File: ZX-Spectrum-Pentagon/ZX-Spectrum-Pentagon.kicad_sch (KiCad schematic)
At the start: 0 parts

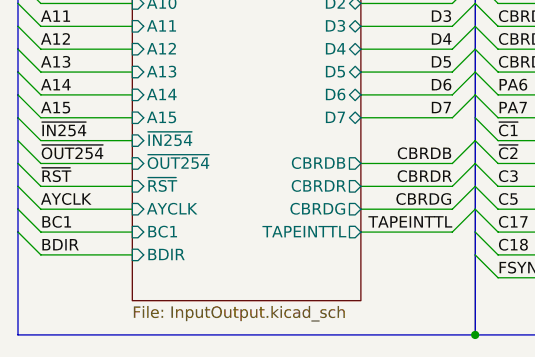
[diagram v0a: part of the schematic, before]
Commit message: add ~{RESET} signal to keyboard
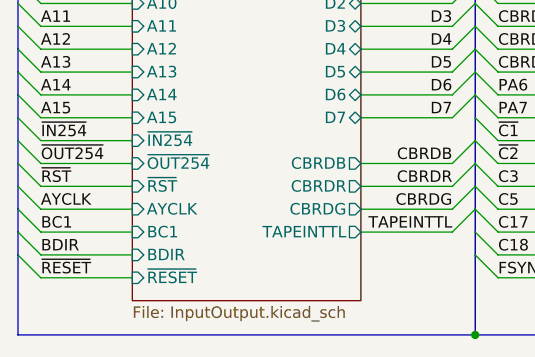
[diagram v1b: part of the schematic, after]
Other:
- sheet InputOutput ports: added ~{RESET}; removed none
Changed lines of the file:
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@@
     (stroke (width 0) (type default) (color 0 0 0 0))
   )
+  (bus_entry (at 25.4 187.96) (size 2.54 2.54)
+    (stroke (width 0) (type default) (color 0 0 0 0))
+  )
   (bus_entry (at 127 114.3) (size -2.54 2.54)
     (stroke (width 0) (type default) (color 0 0 0 0))
@@
     (stroke (width 0) (type default) (color 0 0 0 0))
   )
-  (bus (pts (xy 25.4 185.42) (xy 25.4 196.85))
+  (bus (pts (xy 25.4 185.42) (xy 25.4 187.96))
     (stroke (width 0) (type default) (color 0 0 0 0))
   )
@@
     (stroke (width 0) (type default) (color 0 0 0 0))
   )
+  (wire (pts (xy 27.94 190.5) (xy 38.1 190.5))
+    (stroke (width 0) (type default) (color 0 0 0 0))
+  )
   (bus (pts (xy 127 69.85) (xy 127 71.12))
     (stroke (width 0) (type default) (color 0 0 0 0))
@@
     (stroke (width 0) (type default) (color 0 0 0 0))
   )
+  (bus (pts (xy 25.4 187.96) (xy 25.4 196.85))
+    (stroke (width 0) (type default) (color 0 0 0 0))
+  )
   (wire (pts (xy 78.74 152.4) (xy 88.9 152.4))
     (stroke (width 0) (type default) (color 0 0 0 0))
@@
     (effects (font (size 1.27 1.27)) (justify right bottom))
   )
+  (label "~{RESET}" (at 27.94 190.5 0)
+    (effects (font (size 1.27 1.27)) (justify left bottom))
+  )
   (label "C3" (at 78.74 180.34 0)
     (effects (font (size 1.27 1.27)) (justify left bottom))
@@
       (effects (font (size 1.27 1.27)) (justify right))
     )
+    (pin "~{RESET}" input (at 38.1 190.5 180)
+      (effects (font (size 1.27 1.27)) (justify left))
+    )
   )
   (sheet (at 88.9 104.14) (size 25.4 27.94) (fields_autoplaced)
@@
       (reference "#PWR0102") (unit 1) (value "VCC") (footprint "")
     )
-    (path "/00000000-0000-0000-0000-000062a08194/0e9cb254-d5a6-43df-b938-d4e89e7c4f1b"
-      (reference "#PWR0103") (unit 1) (value "GND") (footprint "")
-    )
     (path "/00000000-0000-0000-0000-000062a08194/c31e7ab1-f89e-4888-8329-6b12abe8b2da"
       (reference "#PWR0104") (unit 1) (value "VCC") (footprint "")
@@
     )
     (path "/00000000-0000-0000-0000-000062a08194/ac0214e0-cfb9-4b53-9214-9139dd989c7d"
-      (reference "JIOKB1") (unit 1) (value "KDATA") (footprint "Connector_PinHeader_2.54mm:PinHeader_1x07_P2.54mm_Vertical")
+      (reference "JIOKB1") (unit 1) (value "KDATA") (footprint "Connector_PinHeader_2.54mm:PinHeader_1x08_P2.54mm_Vertical")
     )
     (path "/00000000-0000-0000-0000-000062a08194/de775720-f7f2-4e8e-8eb2-c9141e64fe25"

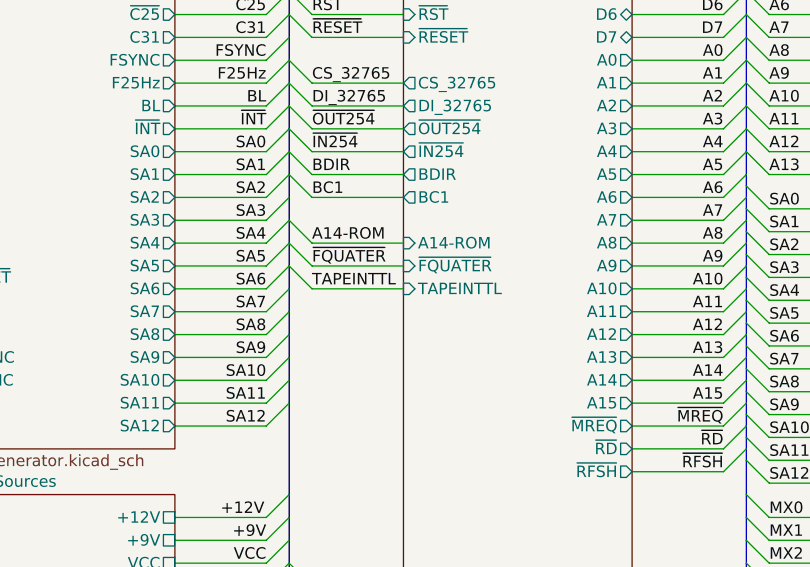
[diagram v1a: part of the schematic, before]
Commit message: add second level delete TYPETTL
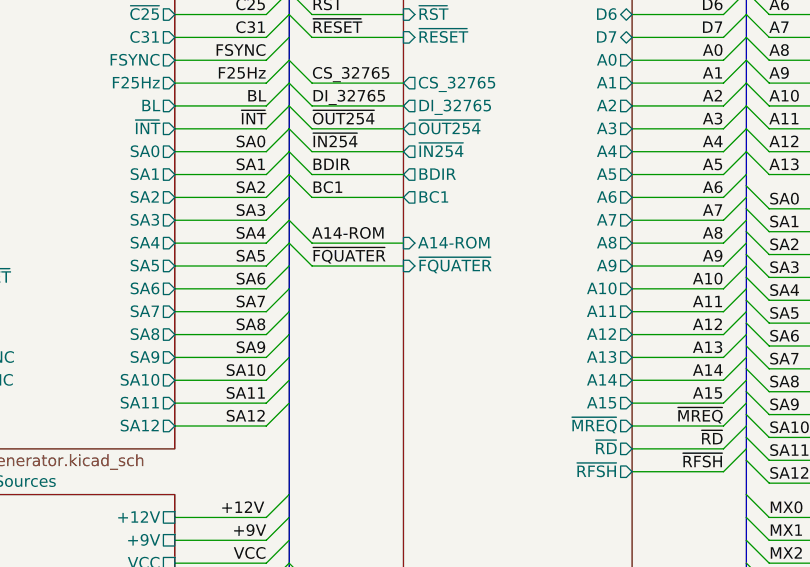
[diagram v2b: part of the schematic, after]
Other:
- sheet CPU ports: added none; removed TAPEINTTL
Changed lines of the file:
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@@
-    (stroke (width 0) (type default) (color 0 0 0 0))
-  )
-  (bus_entry (at 76.2 60.96) (size 2.54 2.54)
     (stroke (width 0) (type default) (color 0 0 0 0))
   )
@@
     (stroke (width 0) (type default) (color 0 0 0 0))
   )
-  (wire (pts (xy 78.74 63.5) (xy 88.9 63.5))
-    (stroke (width 0) (type default) (color 0 0 0 0))
-  )
   (wire (pts (xy 63.5 132.08) (xy 73.66 132.08))
     (stroke (width 0) (type default) (color 0 0 0 0))
@@
   )
   (label "A15" (at 27.94 172.72 0)
-    (effects (font (size 1.27 1.27)) (justify left bottom))
-  )
-  (label "TAPEINTTL" (at 78.74 63.5 0)
     (effects (font (size 1.27 1.27)) (justify left bottom))
   )
@@
       (effects (font (size 1.27 1.27)) (justify left))
     )
-    (pin "TAPEINTTL" input (at 88.9 63.5 180)
-      (effects (font (size 1.27 1.27)) (justify left))
-    )

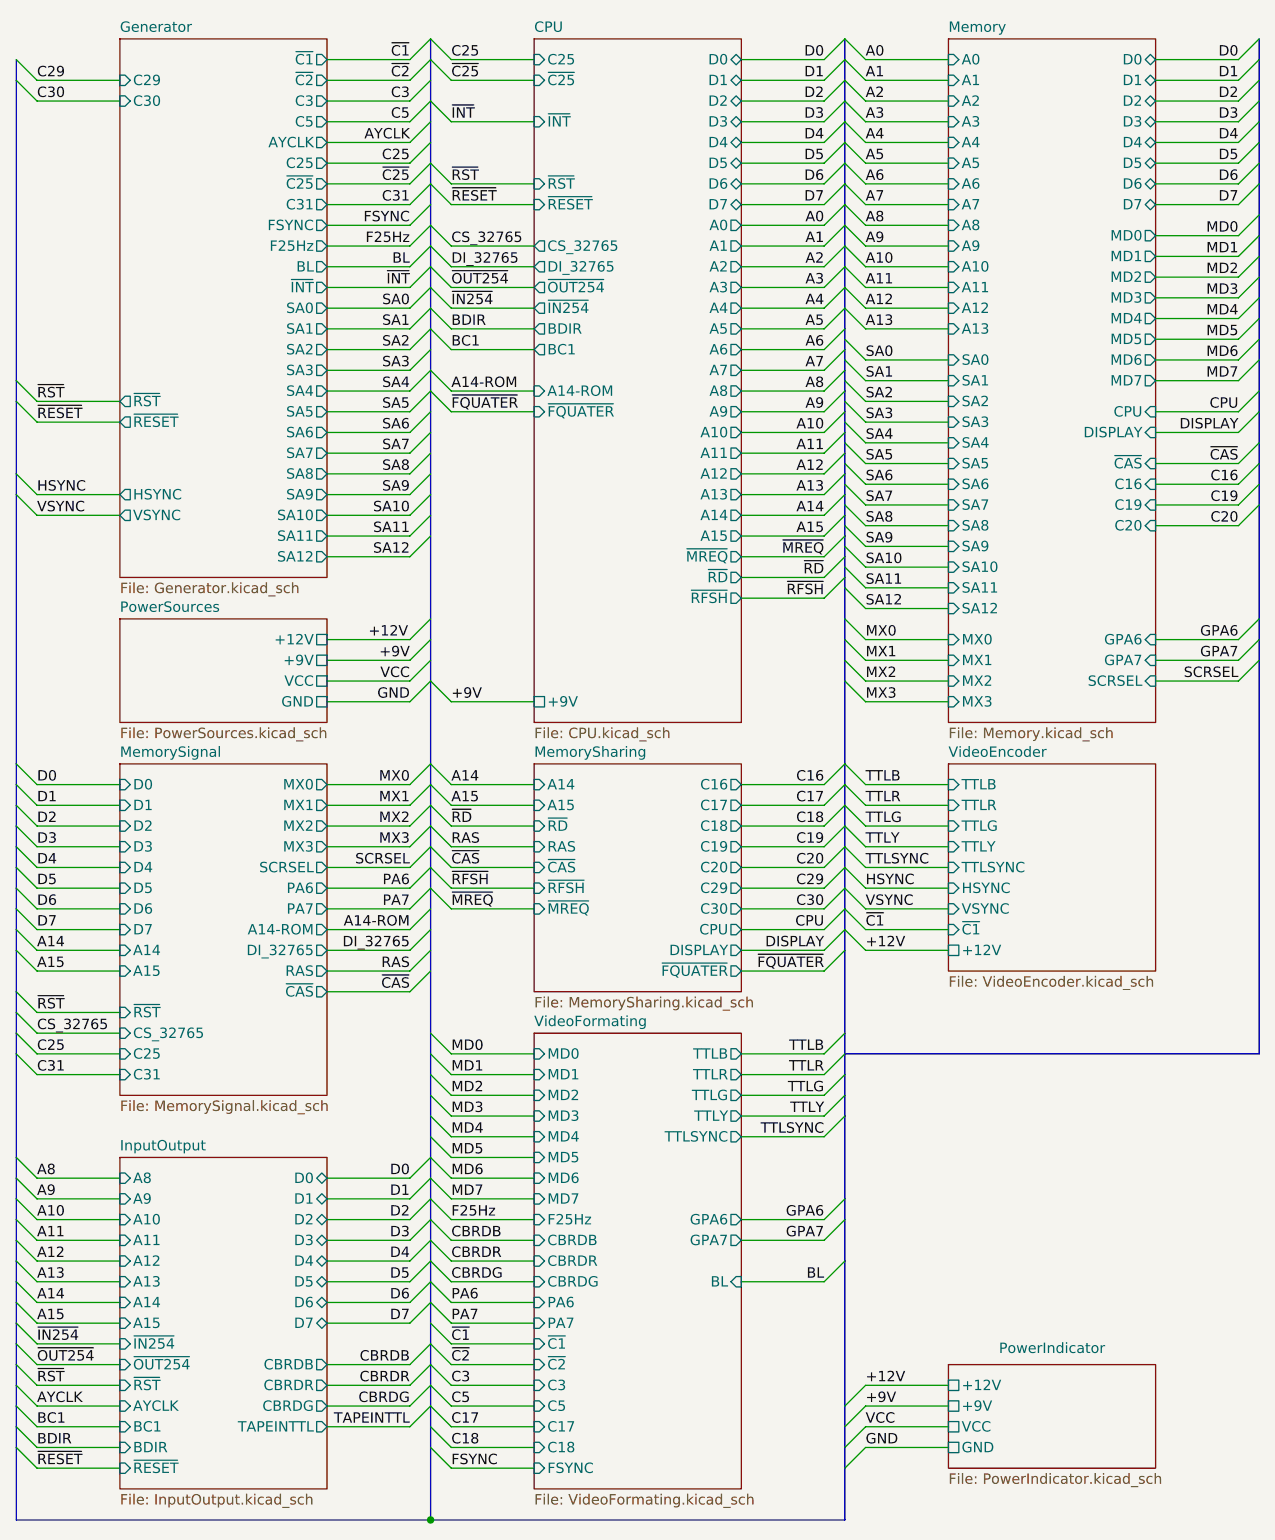
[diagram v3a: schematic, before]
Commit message: migrate ZX-Spectrum-Keyboard_Switch
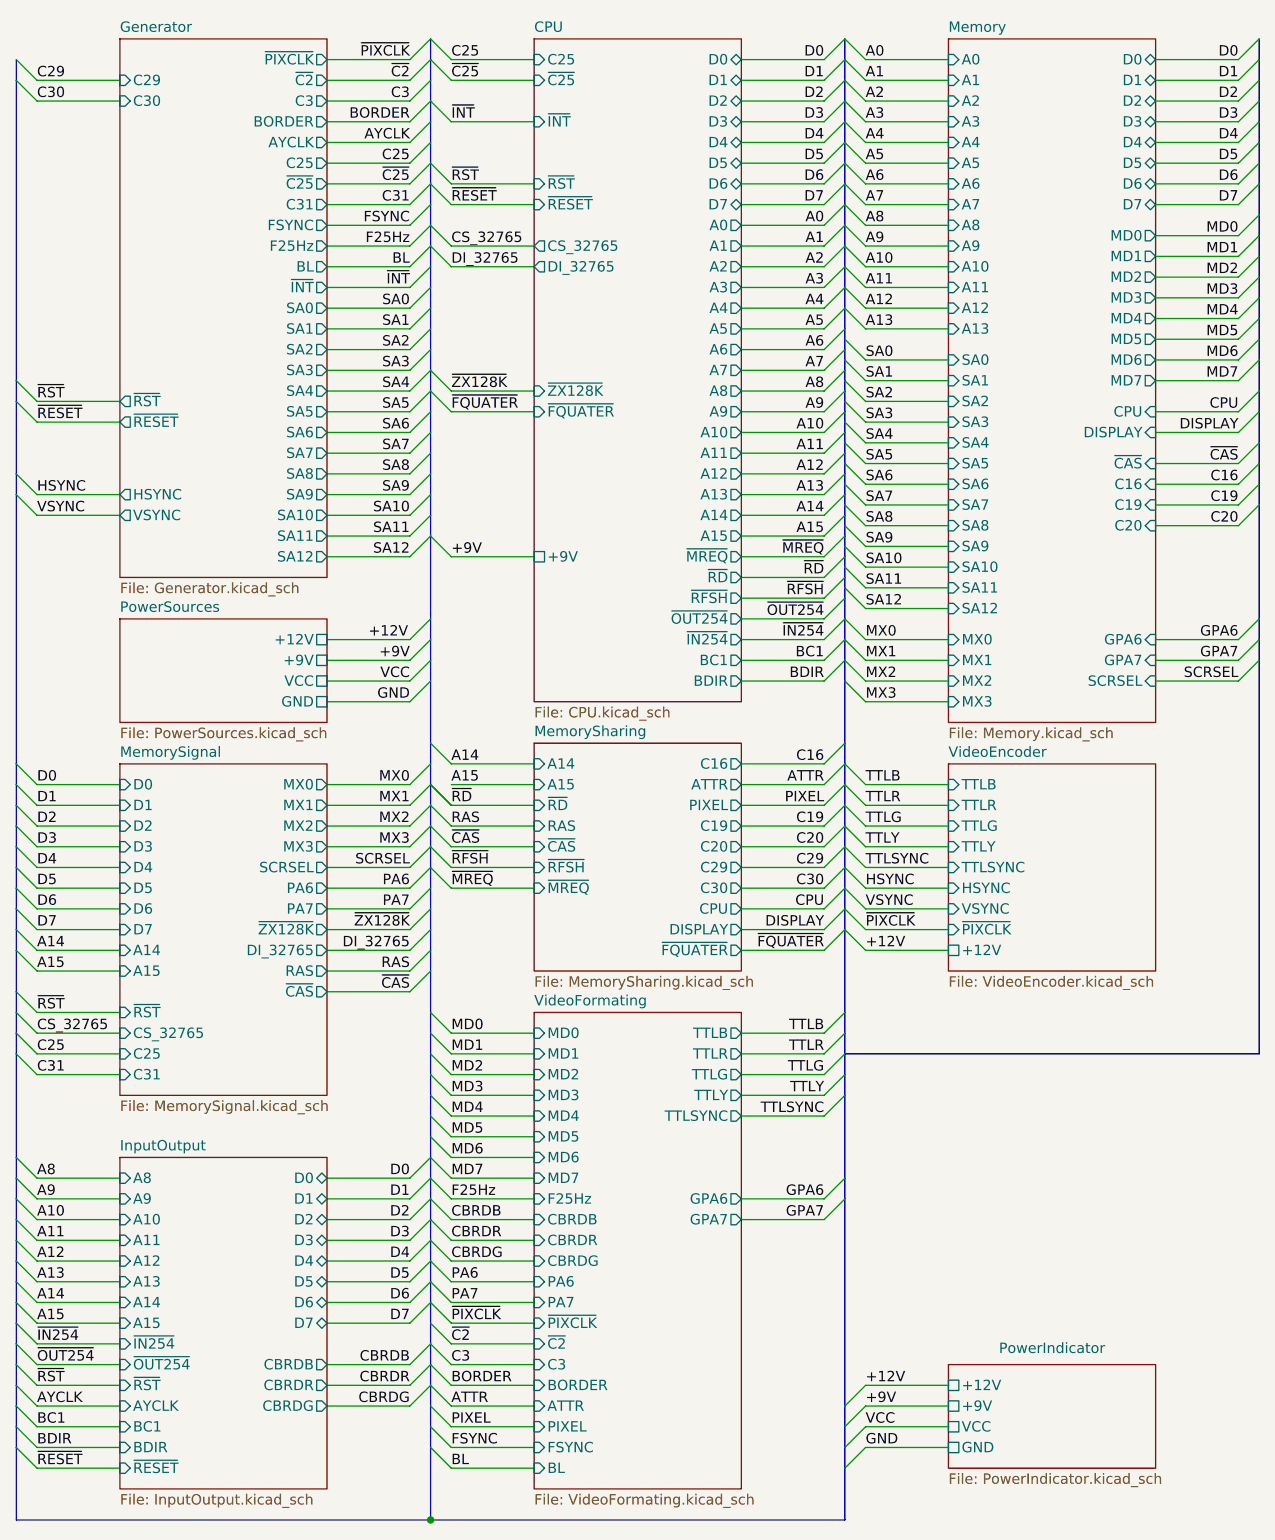
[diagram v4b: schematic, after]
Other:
- sheet CPU ports: added ~{ZX128K}; removed A14-ROM
- sheet Generator ports: added BORDER, ~{PIXCLK}; removed C5, ~{C1}
- sheet InputOutput ports: added none; removed TAPEINTTL
- sheet MemorySharing ports: added ATTR, PIXEL; removed C17, C18
- sheet MemorySignal ports: added ~{ZX128K}; removed A14-ROM
- sheet VideoEncoder ports: added ~{PIXCLK}; removed ~{C1}
- sheet VideoFormating ports: added ATTR, BORDER, PIXEL, ~{PIXCLK}; removed C17, C18, C5, ~{C1}
